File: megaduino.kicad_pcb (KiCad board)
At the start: 2 copper layers, 48.9 x 54 mm, 36 parts, among them J1 Conn_01x20_Female, J2 Conn_01x20_Female, J3 Conn_01x13_Male, J4 Conn_01x02_Male, J5 Conn_01x04_Male, Q1 RFD14N05L, Q2 RFD14N05L, U1 LMV324, U2 MCP2562-E-SN, U3 LMV324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

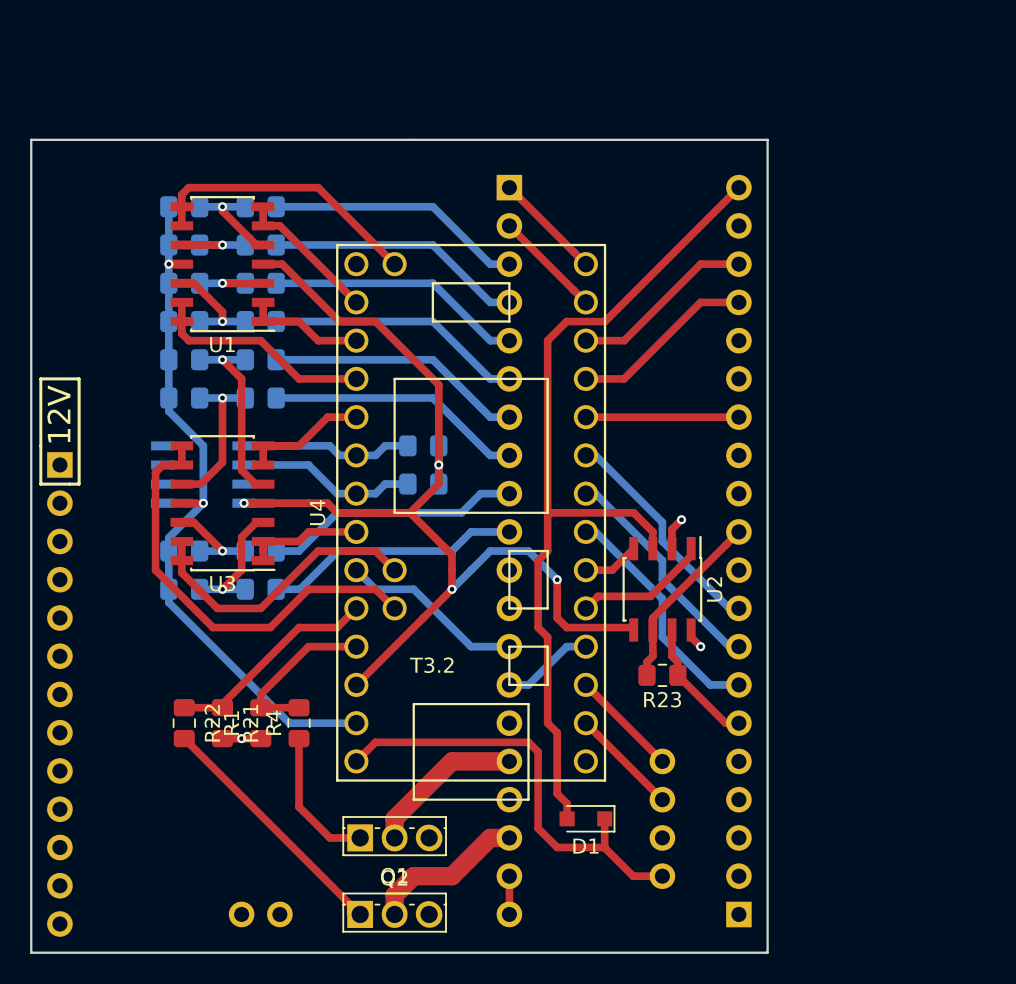
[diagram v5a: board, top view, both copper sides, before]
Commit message: add proto area
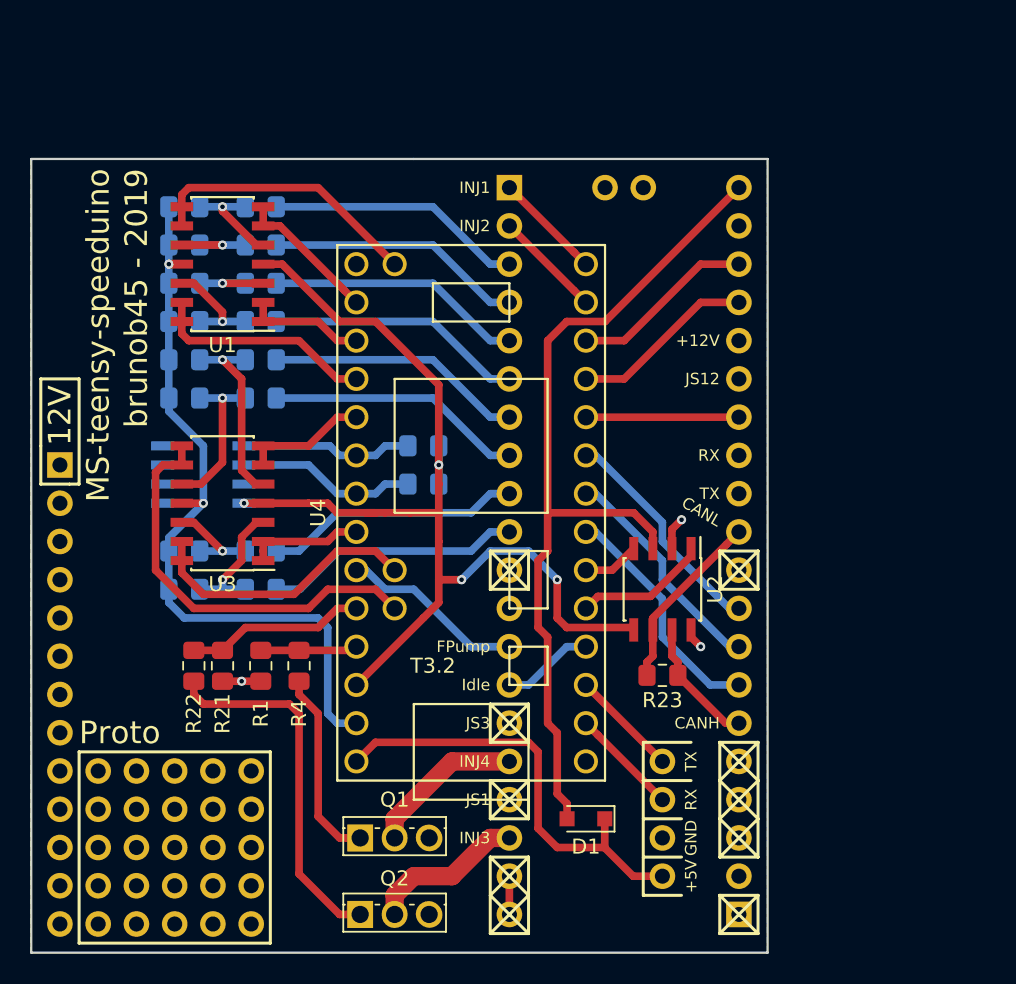
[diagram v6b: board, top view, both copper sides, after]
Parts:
- added REF**: PinHeader_1x05_P2.54mm_Vertical, Connector_PinHeader_2.54mm:PinHeader_1x05_P2.54mm_Vertical, B.Cu at (122.6, 117.5)
- added REF**: PinHeader_1x05_P2.54mm_Vertical, Connector_PinHeader_2.54mm:PinHeader_1x05_P2.54mm_Vertical, B.Cu at (122.6, 114.9)
- added REF**: PinHeader_1x05_P2.54mm_Vertical, Connector_PinHeader_2.54mm:PinHeader_1x05_P2.54mm_Vertical, B.Cu at (122.6, 112.4)
- added REF**: PinHeader_1x05_P2.54mm_Vertical, Connector_PinHeader_2.54mm:PinHeader_1x05_P2.54mm_Vertical, B.Cu at (122.6, 109.9)
- added REF**: PinHeader_1x05_P2.54mm_Vertical, Connector_PinHeader_2.54mm:PinHeader_1x05_P2.54mm_Vertical, B.Cu at (122.6, 107.3)
- J3: value Conn_01x13_Male -> Conn_01x12_Male
- moved J4 54.0 mm to (156.2, 68.6)
- moved R22 3.86 mm to (128.9, 100.3)
- moved R1 3.81 mm to (133.3, 100.3)
- moved R21 3.81 mm to (130.8, 100.3)
- moved R4 3.81 mm to (135.9, 100.3)
- moved R5 2.54 mm to (133.3, 69.8)
- moved R6 2.54 mm to (128.3, 69.8)
- moved R7 2.54 mm to (133.3, 72.4)
- moved R8 2.54 mm to (128.3, 72.4)
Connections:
- net Net-(J1-Pad1) renamed Vsyn
- net Net-(J1-Pad3) renamed CGMXFC
- net Net-(J1-Pad4) renamed OSC2
- net Net-(J1-Pad5) renamed OSC1
- net Net-(J2-Pad11) renamed Vref
- J3 pad 13: Net-(J3-Pad13) -> (no net)
- R5 pad 1: AD1 -> AD0
- R7 pad 1: AD0 -> AD1
- U1 pad 10: Net-(R5-Pad2) -> Net-(R7-Pad2)
- U1 pad 5: Net-(R7-Pad2) -> Net-(R5-Pad2)
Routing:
- net Net-(Q2-Pad1): track 16.2 -> 25.3 mm
- net INJ4: track 11.1 -> 6.45 mm
- net Net-(Q1-Pad1): track 8.81 -> 13.4 mm
- net GNDA: track 46.2 -> 49.6 mm
- net INJ3: track 14.3 -> 11.9 mm
- net Net-(R7-Pad2): track 6.95 -> 5.73 mm
- net Net-(R5-Pad2): track 5.73 -> 6.95 mm
- net A5: track 28.7 -> 27.7 mm
- net A6: track 19.7 -> 19.0 mm
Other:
- board size 48.9 x 54 mm -> 48.9 x 52.7 mm
- board text added: "+12V"
- board text added: "+5V"
- board text added: "CANH"
- board text added: "CANL"
- board text added: "FPump"
- board text added: "GND"
- board text added: "INJ1"
- board text added: "INJ2"
- board text added: "INJ3"
- board text added: "INJ4"
- board text added: "Idle"
- board text added: "JS1"
- board text added: "JS12"
- board text added: "JS3"
- board text added: "MS-teensy-speeduino"
- board text added: "Proto"
- board text added: "RX"
- board text added: "TX"
- board text added: "brunob45 - 2019"

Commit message: final version 2.1
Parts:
- removed REF** (x5): PinHeader_1x05_P2.54mm_Vertical, Connector_PinHeader_2.54mm:PinHeader_1x05_P2.54mm_Vertical
- moved J4 36.3 mm to (120.0, 71.1), turned to 0 degrees
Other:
- board text added: "ANALOG0..7"
- board text added: "ECL"
- board text added: "FAN"
- board text added: "IGN1"
- board text added: "IGN2"
- board text added: "IRQ1"
- board text added: "IRQ2"
- board text removed: "Proto"

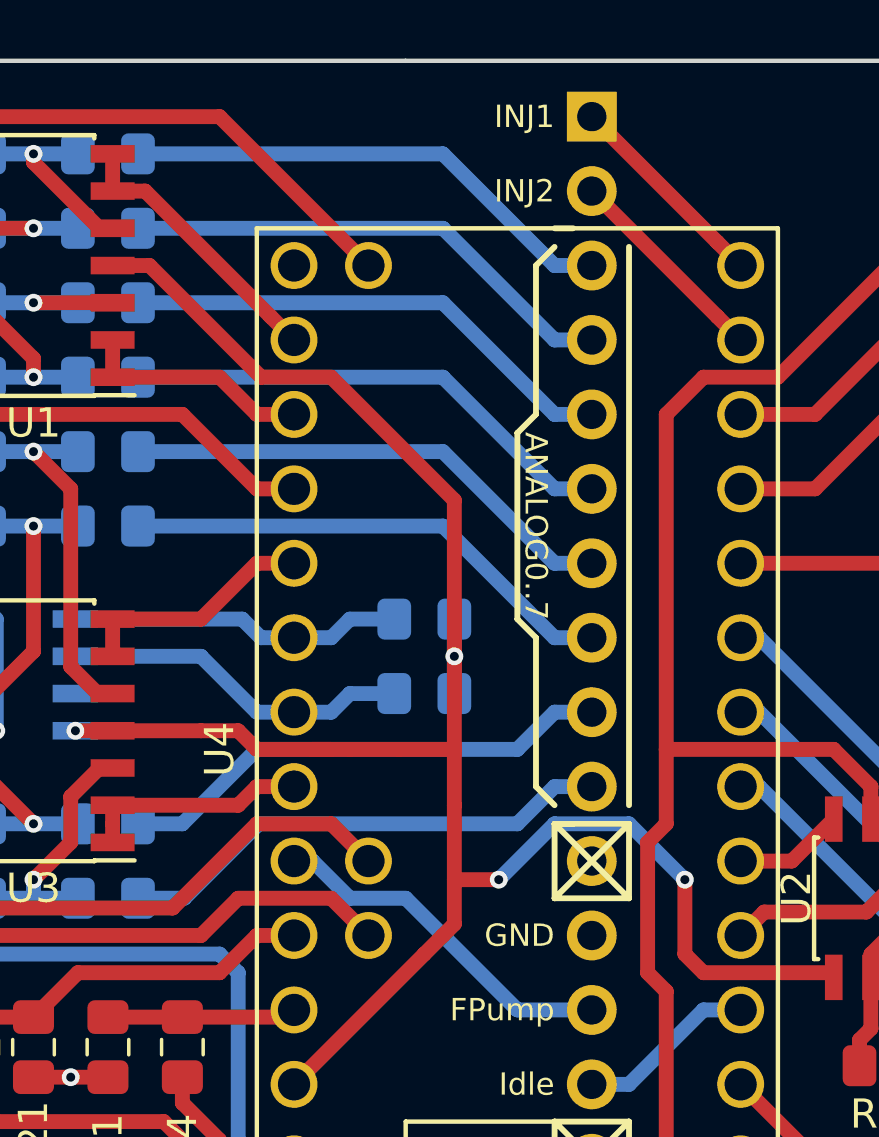
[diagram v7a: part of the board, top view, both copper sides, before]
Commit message: add pull-up resistors on injector outputs
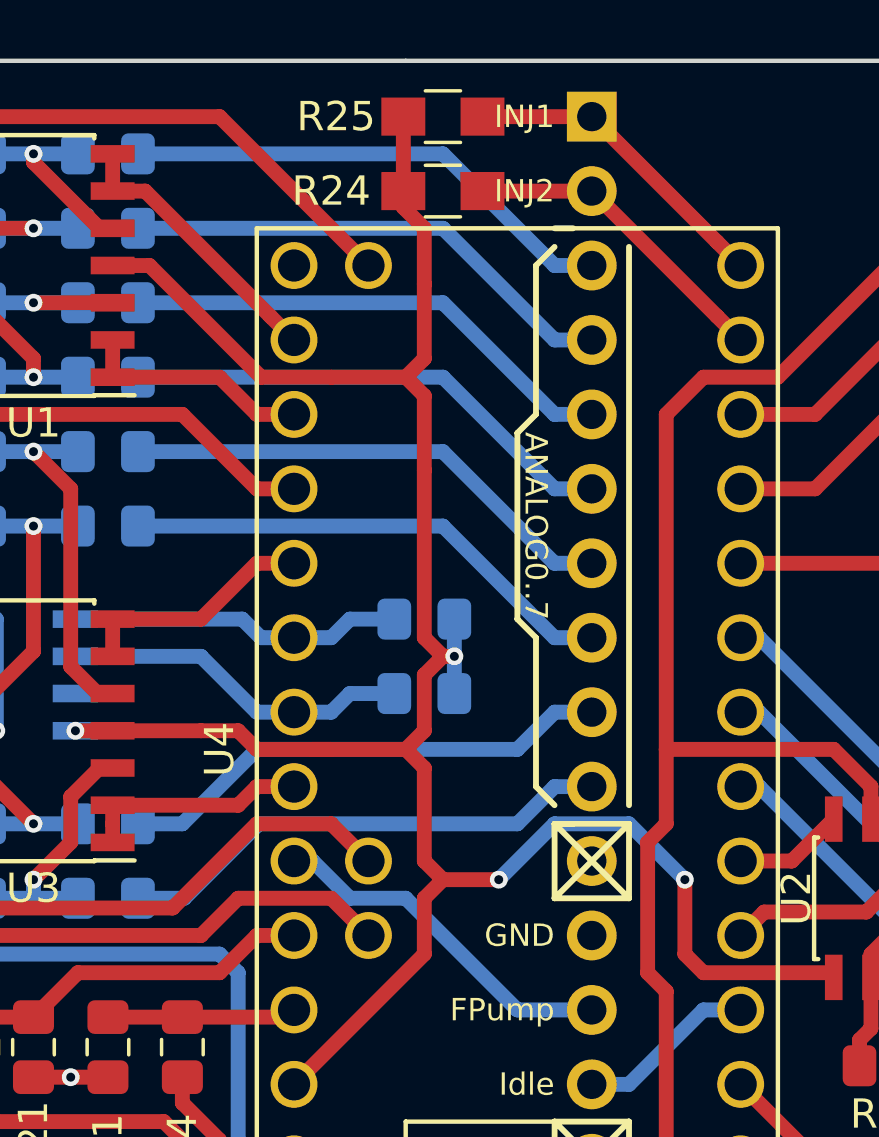
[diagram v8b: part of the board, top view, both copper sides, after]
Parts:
- added R24: 1k, Resistors_SMD:R_0805_HandSoldering, F.Cu at (144.8, 71.1)
- added R25: 1k, Resistors_SMD:R_0805_HandSoldering, F.Cu at (144.8, 68.6)
- J3: value Conn_01x12_Male -> Conn_01x13_Male
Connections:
- J1 pad 1: Vsyn -> (no net)
- J1 pad 10: JS7 -> (no net)
- J1 pad 12: TX -> (no net)
- J1 pad 13: RX -> (no net)
- J1 pad 15: JS12 -> (no net)
- J1 pad 16: +12V -> (no net)
- J1 pad 3: CGMXFC -> (no net)
- J1 pad 4: OSC2 -> (no net)
- J1 pad 5: OSC1 -> (no net)
- J2 pad 11: Vref -> (no net)
- J2 pad 15: JS3 -> (no net)
- J2 pad 17: JS1 -> (no net)
- J3 pad 1: Net-(J3-Pad1) -> (no net)
- J3 pad 10: Net-(J3-Pad10) -> (no net)
- J3 pad 11: Net-(J3-Pad11) -> (no net)
- J3 pad 12: Net-(J3-Pad12) -> (no net)
- J3 pad 2: Net-(J3-Pad2) -> (no net)
- J3 pad 3: Net-(J3-Pad3) -> (no net)
- J3 pad 4: Net-(J3-Pad4) -> (no net)
- J3 pad 5: Net-(J3-Pad5) -> (no net)
- J3 pad 6: Net-(J3-Pad6) -> (no net)
- J3 pad 7: Net-(J3-Pad7) -> (no net)
- J3 pad 8: Net-(J3-Pad8) -> (no net)
- J3 pad 9: Net-(J3-Pad9) -> (no net)
- U4 pad 20: D13 -> (no net)
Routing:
- net +3V3: track 70.9 -> 81.7 mm
- net INJ1: track 7.18 -> 11.1 mm
- net INJ2: track 7.18 -> 10.9 mm
